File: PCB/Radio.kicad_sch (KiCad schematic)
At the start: 3 parts, among them J8 Conn_Coaxial, U8 RFM95W-915S2

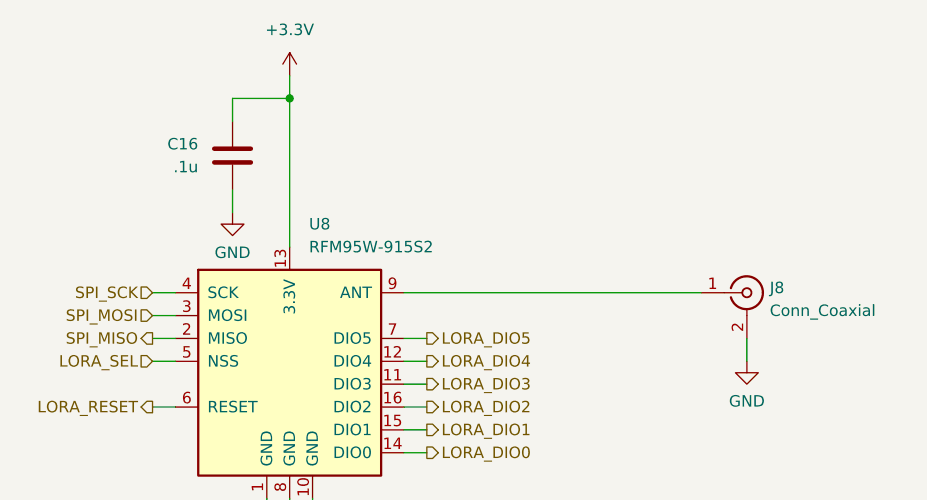
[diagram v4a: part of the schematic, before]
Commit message: Fixed component annotation Updated BOM to reflect the pyro channel changes Updates Production files
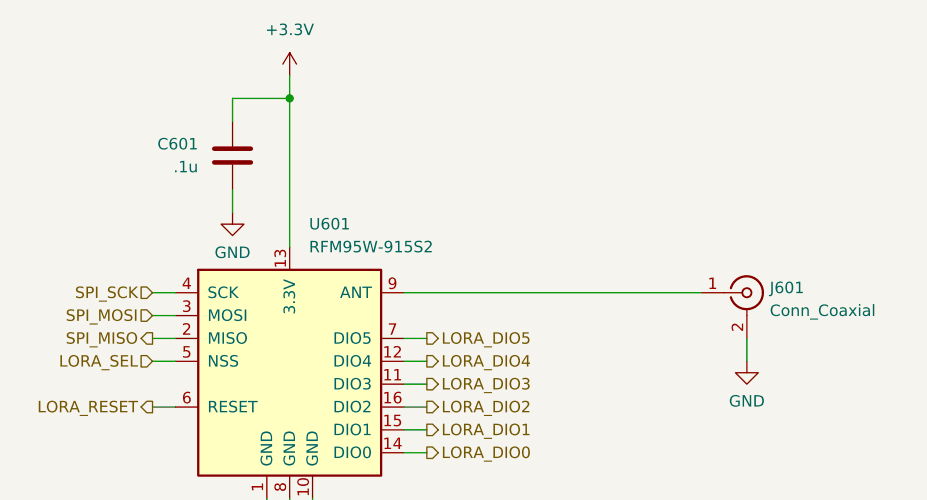
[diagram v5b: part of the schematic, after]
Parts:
- renumbered C16 to C601, J8 to J601, U8 to U601
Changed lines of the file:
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@@
 		(dnp no)
 		(fields_autoplaced yes)
-		(property "Reference" "#PWR056"
+		(property "Reference" "#PWR0601"
 			(at 115.57 58.42 0)
 			(effects
@@
 			(project "Flight Computer"
 				(path "/4254ccd1-49f4-4fe6-9bf7-ccb200d73af4/b5b3f2b6-4604-4088-8488-54d61b2ee536"
-					(reference "#PWR056")
+					(reference "#PWR0601")
 					(unit 1)
 				)
@@
 		(dnp no)
 		(fields_autoplaced yes)
-		(property "Reference" "#PWR057"
+		(property "Reference" "#PWR0602"
 			(at 109.22 76.2 0)
 			(effects
@@
 			(project "Flight Computer"
 				(path "/4254ccd1-49f4-4fe6-9bf7-ccb200d73af4/b5b3f2b6-4604-4088-8488-54d61b2ee536"
-					(reference "#PWR057")
+					(reference "#PWR0602")
 					(unit 1)
 				)
@@
 		(on_board yes)
 		(dnp no)
-		(property "Reference" "C16"
+		(property "Reference" "C601"
 			(at 105.41 62.2299 0)
 			(effects
@@
 			(project ""
 				(path "/4254ccd1-49f4-4fe6-9bf7-ccb200d73af4/b5b3f2b6-4604-4088-8488-54d61b2ee536"
-					(reference "C16")
+					(reference "C601")
 					(unit 1)
 				)
@@
 		(dnp no)
 		(fields_autoplaced yes)
-		(property "Reference" "J8"
+		(property "Reference" "J601"
 			(at 168.91 78.1985 0)
 			(effects
@@
 			(project "Flight Computer"
 				(path "/4254ccd1-49f4-4fe6-9bf7-ccb200d73af4/b5b3f2b6-4604-4088-8488-54d61b2ee536"
-					(reference "J8")
+					(reference "J601")
 					(unit 1)
 				)
@@
 		(dnp no)
 		(fields_autoplaced yes)
-		(property "Reference" "U8"
+		(property "Reference" "U601"
 			(at 117.7133 71.12 0)
 			(effects
@@
 			(project ""
 				(path "/4254ccd1-49f4-4fe6-9bf7-ccb200d73af4/b5b3f2b6-4604-4088-8488-54d61b2ee536"
-					(reference "U8")
+					(reference "U601")
 					(unit 1)
 				)
@@
 		(dnp no)
 		(fields_autoplaced yes)
-		(property "Reference" "#PWR059"
+		(property "Reference" "#PWR0604"
 			(at 115.57 113.03 0)
 			(effects
@@
 			(project "Flight Computer"
 				(path "/4254ccd1-49f4-4fe6-9bf7-ccb200d73af4/b5b3f2b6-4604-4088-8488-54d61b2ee536"
-					(reference "#PWR059")
+					(reference "#PWR0604")
 					(unit 1)
 				)
@@
 		(dnp no)
 		(fields_autoplaced yes)
-		(property "Reference" "#PWR058"
+		(property "Reference" "#PWR0603"
 			(at 166.37 92.71 0)
 			(effects
@@
 			(project "Flight Computer"
 				(path "/4254ccd1-49f4-4fe6-9bf7-ccb200d73af4/b5b3f2b6-4604-4088-8488-54d61b2ee536"
-					(reference "#PWR058")
-					(unit 1)
-				)
+					(reference "#PWR0603")
+					(unit 1)
+				)

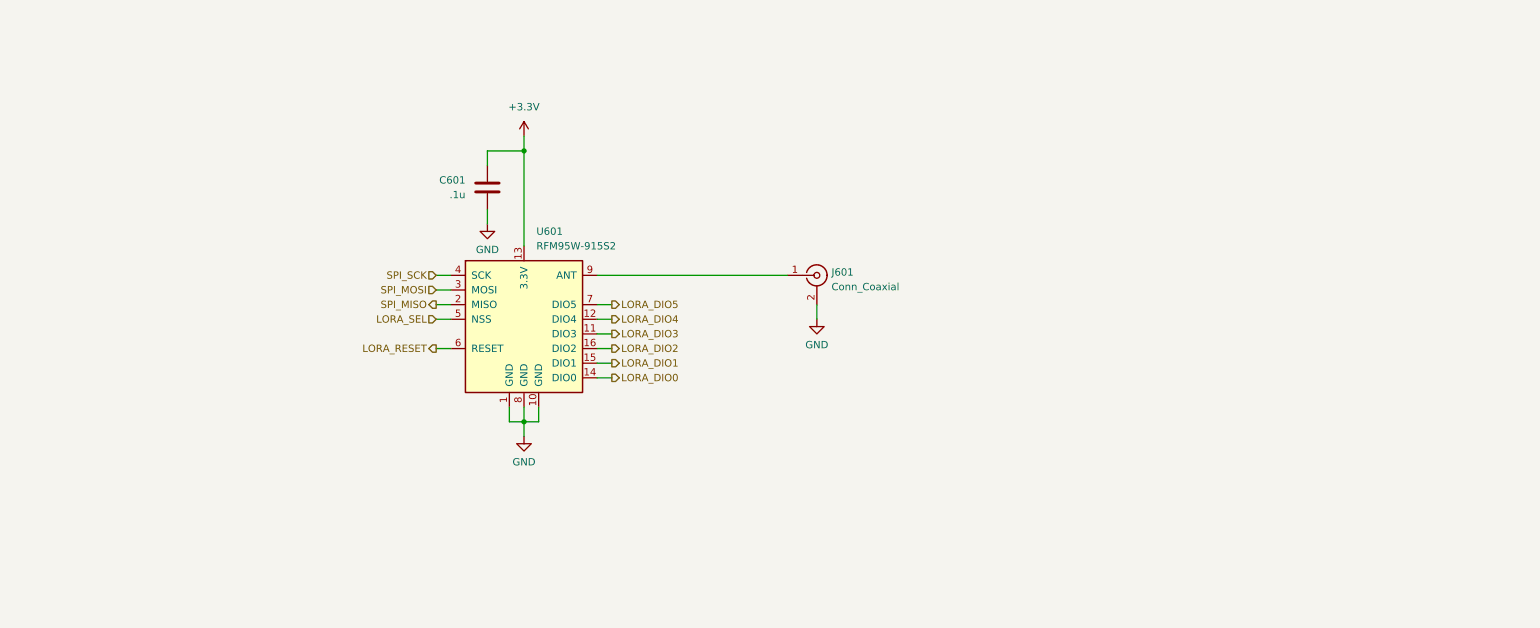
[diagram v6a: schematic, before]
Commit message: Replaced the radio in the schematic
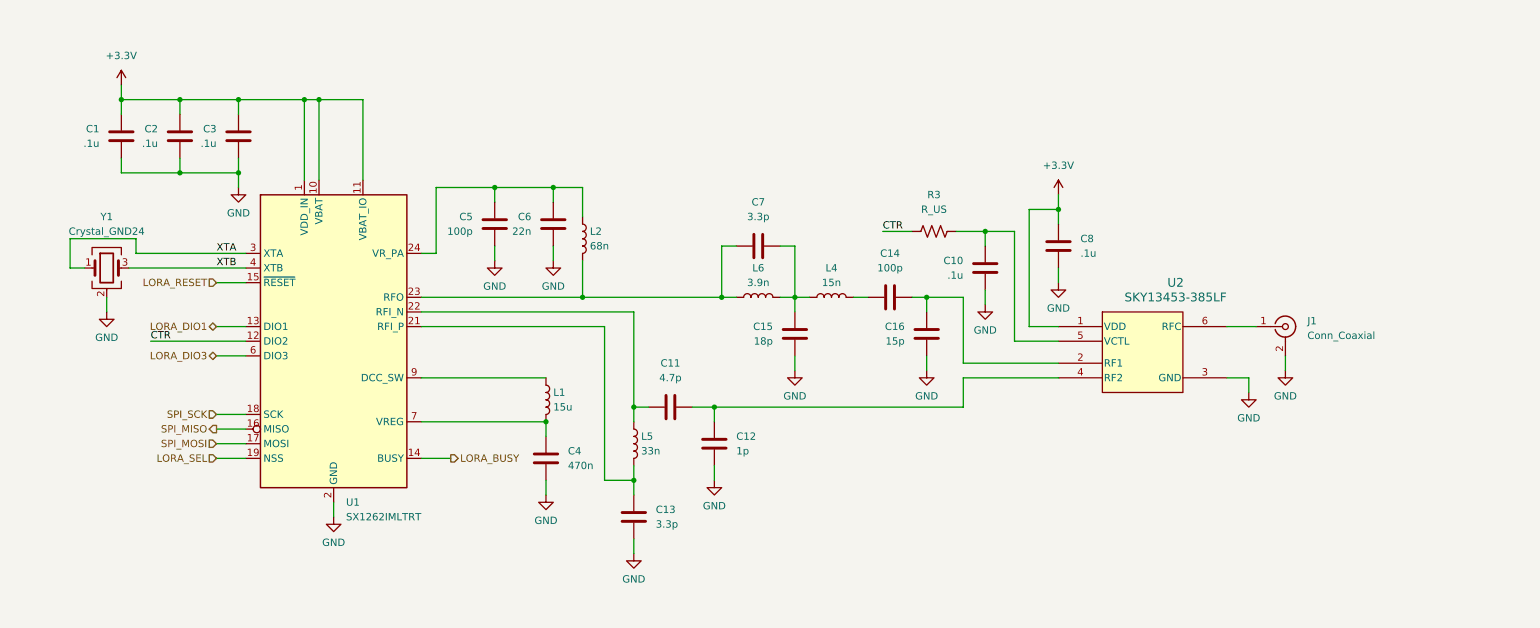
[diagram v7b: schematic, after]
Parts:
- removed C601: .1u, Capacitor_SMD:C_0603_1608Metric_Pad1.08x0.95mm_HandSolder, symbol Device:C
- removed J601: Conn_Coaxial, Connector_Coaxial:SMA_Samtec_SMA-J-P-H-ST-EM1_EdgeMount, symbol Connector:Conn_Coaxial
- removed U601: RFM95W-915S2, RF_Module:HOPERF_RFM9XW_SMD, symbol RF_Module:RFM95W-915S2
- added C1, C10, C2, C3, C8: .1u, symbol Device:C
- added C11: 4.7p, symbol Device:C
- added C12: 1p, symbol Device:C
- added C13, C7: 3.3p, symbol Device:C
- added C14, C5: 100p, symbol Device:C
- added C15: 18p, symbol Device:C
- added C16: 15p, symbol Device:C
- added C4: 470n, symbol Device:C
- added C6: 22n, symbol Device:C
- added J1: Conn_Coaxial, Connector_Coaxial:SMA_Samtec_SMA-J-P-H-ST-EM1_EdgeMount, symbol Connector:Conn_Coaxial
- added L1: 15u, symbol Device:L
- added L2: 68n, symbol Device:L
- added L4: 15n, symbol Device:L
- added L5: 33n, symbol Device:L
- added L6: 3.9n, symbol Device:L
- added R3: R_US, symbol Device:R_US
- added U1: SX1262IMLTRT, Package_DFN_QFN:QFN-24-1EP_4x4mm_P0.5mm_EP2.6x2.6mm, symbol RF:SX1262IMLTRT
- added U2: SKY13453-385LF, QFN_453-385LF_SKY, symbol SKY13453-385LF:SKY13453-385LF
- added Y1: Crystal_GND24, symbol Device:Crystal_GND24
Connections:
- net +3.3V: now also C1.1, C2.1, C3.1, C8.1, U1.1 (VDD_IN), U1.10 (VBAT), U1.11 (VBAT_IO), U2.1 (VDD)
- net GND: now also C1.2, C10.2, C12.2, C13.2, C15.2, C16.2, C2.2, C3.2, C4.2, C5.2, C6.2, C8.2, J1.2 (Ext), U1.2 (GND), U1.20 (GND), U1.25 (GND), U1.5 (GND), U1.8 (GND), U2.3 (GND), Y1.2 (G), Y1.4 (G)
- net LORA_DIO1: now also U1.13 (DIO1)
- net LORA_DIO3: now also U1.6 (DIO3)
- net LORA_RESET: now also U1.15 (~{RESET})
- net LORA_SEL: now also U1.19 (NSS)
- net SPI_MISO: now also U1.16 (MISO)
- net SPI_MOSI: now also U1.17 (MOSI)
- net SPI_SCK: now also U1.18 (SCK)
- new net: C13.1, L5.2, U1.21 (RFI_P)
- new net: C11.2, L5.1, U1.22 (RFI_N)
- new net: C7.1, L2.2, L6.1, U1.23 (RFO)
- new net: C5.1, C6.1, L2.1, U1.24 (VR_PA)
- new net: C4.1, L1.2, U1.7 (VREG)
- new net: L1.1, U1.9 (DCC_SW)
- new net: C14.2, L4.1
- new net: C15.1, C7.2, L4.2, L6.2
- new net: C10.1, R3.2, U2.5 (VCTL)
- new net: C11.1, C12.1, U2.4 (RF2)
- new net: C14.1, C16.1, U2.2 (RF1)
- new net: J1.1 (In), U2.6 (RFC)
- new net CTR: R3.1, U1.12 (DIO2)
- new net LORA_BUSY: U1.14 (BUSY)
- new net XTA: U1.3 (XTA), Y1.1
- new net XTB: U1.4 (XTB), Y1.3

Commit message: - Swapped out 2 LED's for neopixels- Added reverse polarity protection- Replaced Radio module with deticated IC and passives
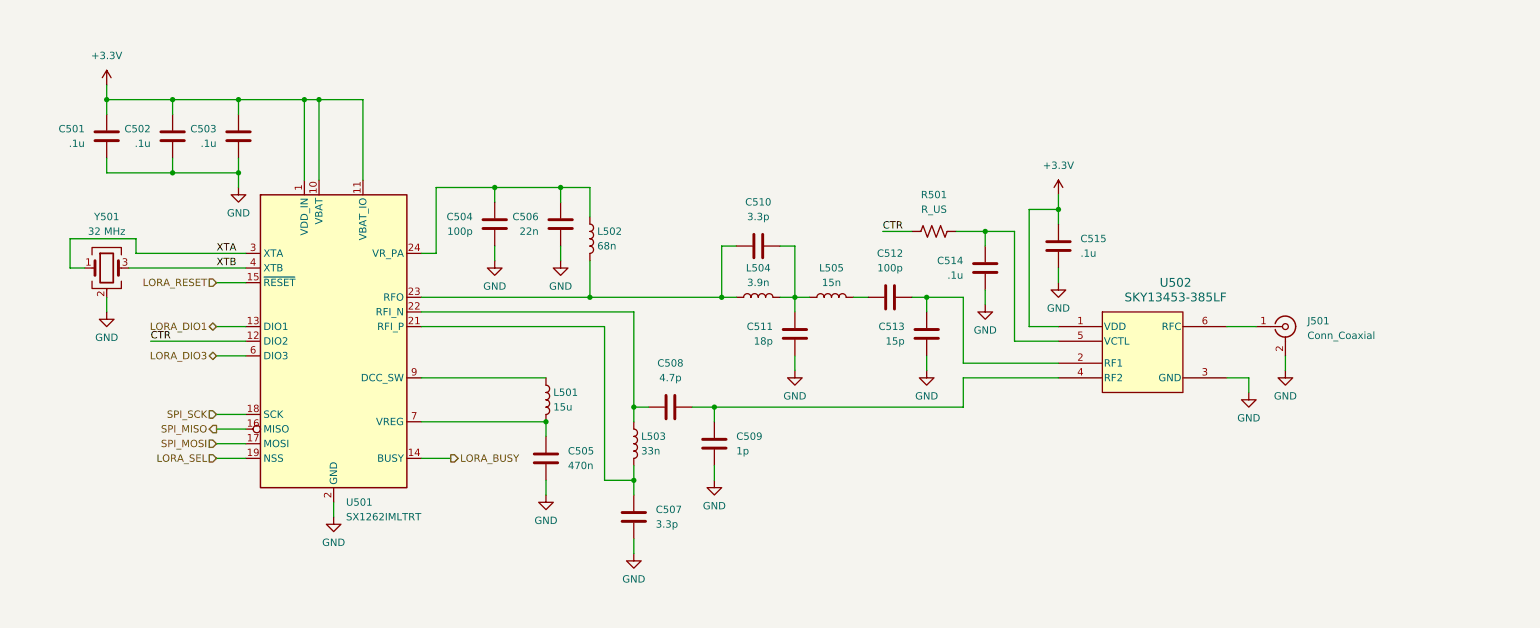
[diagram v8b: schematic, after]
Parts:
- C501: renamed from C1; footprint (none) -> Capacitor_SMD:C_0603_1608Metric_Pad1.08x0.95mm_HandSolder
- C502: renamed from C2; footprint (none) -> Capacitor_SMD:C_0603_1608Metric_Pad1.08x0.95mm_HandSolder
- C503: renamed from C3; footprint (none) -> Capacitor_SMD:C_0603_1608Metric_Pad1.08x0.95mm_HandSolder
- C504: renamed from C5; footprint (none) -> Capacitor_SMD:C_0603_1608Metric_Pad1.08x0.95mm_HandSolder
- C505: renamed from C4; footprint (none) -> Capacitor_SMD:C_0603_1608Metric_Pad1.08x0.95mm_HandSolder
- C506: renamed from C6; footprint (none) -> Capacitor_SMD:C_0603_1608Metric_Pad1.08x0.95mm_HandSolder
- C507: renamed from C13; footprint (none) -> Capacitor_SMD:C_0603_1608Metric_Pad1.08x0.95mm_HandSolder
- C508: renamed from C11; footprint (none) -> Capacitor_SMD:C_0603_1608Metric_Pad1.08x0.95mm_HandSolder
- C509: renamed from C12; footprint (none) -> Capacitor_SMD:C_0603_1608Metric_Pad1.08x0.95mm_HandSolder
- C510: renamed from C7; footprint (none) -> Capacitor_SMD:C_0603_1608Metric_Pad1.08x0.95mm_HandSolder
- C511: renamed from C15; footprint (none) -> Capacitor_SMD:C_0603_1608Metric_Pad1.08x0.95mm_HandSolder
- C512: renamed from C14; footprint (none) -> Capacitor_SMD:C_0603_1608Metric_Pad1.08x0.95mm_HandSolder
- C513: renamed from C16; footprint (none) -> Capacitor_SMD:C_0603_1608Metric_Pad1.08x0.95mm_HandSolder
- C514: renamed from C10; footprint (none) -> Capacitor_SMD:C_0603_1608Metric_Pad1.08x0.95mm_HandSolder
- C515: renamed from C8; footprint (none) -> Capacitor_SMD:C_0603_1608Metric_Pad1.08x0.95mm_HandSolder
- L501: renamed from L1; footprint (none) -> Inductor_SMD:L_0603_1608Metric_Pad1.05x0.95mm_HandSolder
- L502: renamed from L2; footprint (none) -> Inductor_SMD:L_0603_1608Metric_Pad1.05x0.95mm_HandSolder
- L503: renamed from L5; footprint (none) -> Inductor_SMD:L_0603_1608Metric_Pad1.05x0.95mm_HandSolder
- L504: renamed from L6; footprint (none) -> Inductor_SMD:L_0603_1608Metric_Pad1.05x0.95mm_HandSolder
- L505: renamed from L4; footprint (none) -> Inductor_SMD:L_0603_1608Metric_Pad1.05x0.95mm_HandSolder
- R501: renamed from R3; footprint (none) -> Resistor_SMD:R_0603_1608Metric_Pad0.98x0.95mm_HandSolder
- U502: renamed from U2; footprint QFN_453-385LF_SKY -> imported:QFN_453-385LF_SKY
- Y501: renamed from Y1; value Crystal_GND24 -> 32 MHz; footprint (none) -> Crystal:Crystal_SMD_2016-4Pin_2.0x1.6mm
- renumbered J1 to J501, U1 to U501
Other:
- moved on the sheet: C501, C502, C506, L502
